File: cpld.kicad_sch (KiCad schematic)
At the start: 9 parts, among them J2 Conn_01x06_Pin, U6 ATF1508AS-10AU100

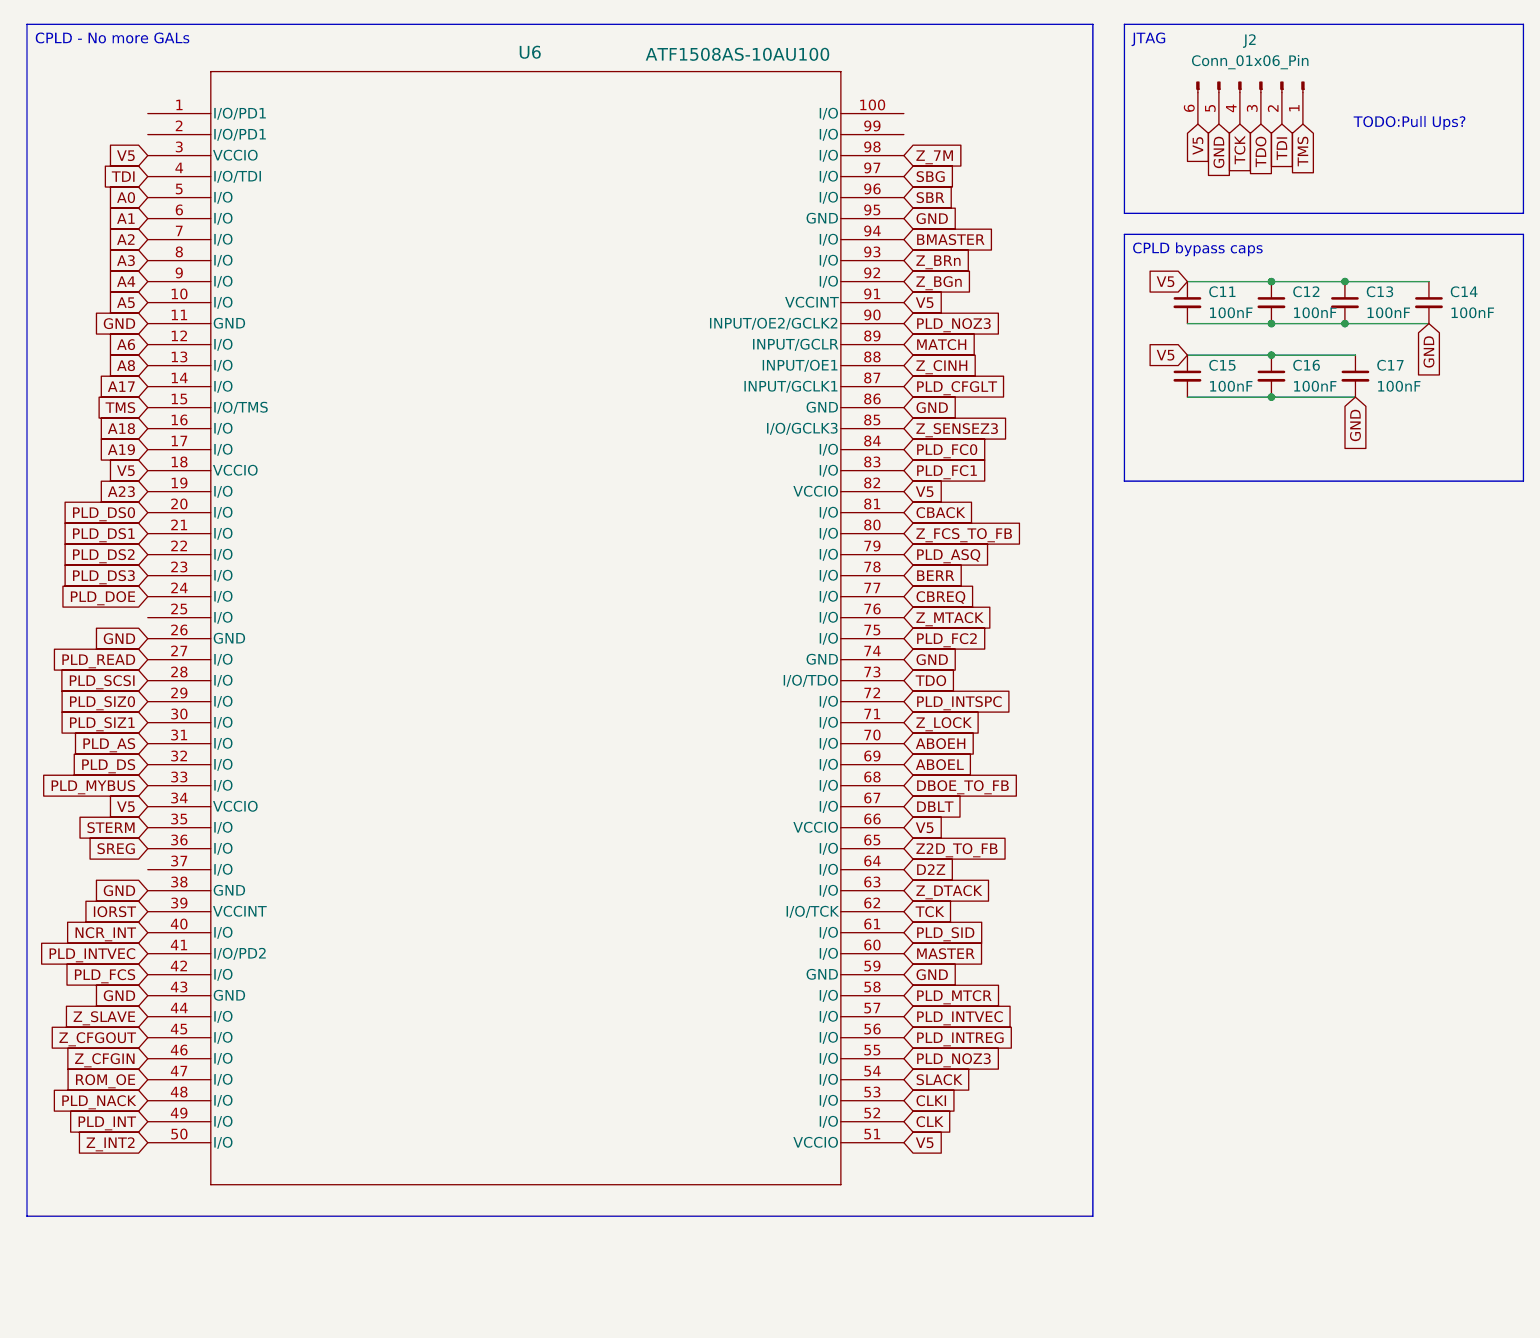
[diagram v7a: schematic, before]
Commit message: Incorporate Feedback from LIV2
- Move CLK, CLKI, Z_7M to GCLK1, GCLK2, GCLK3
  as they are connected to all macro cells.
- OE1 and GCLR on the 1508 are input only, move FC0/FC1 there.

Also found two duplicate signals on the ATF1508, consolidated them.
This leaves us with 8 free I/Os at the moment.
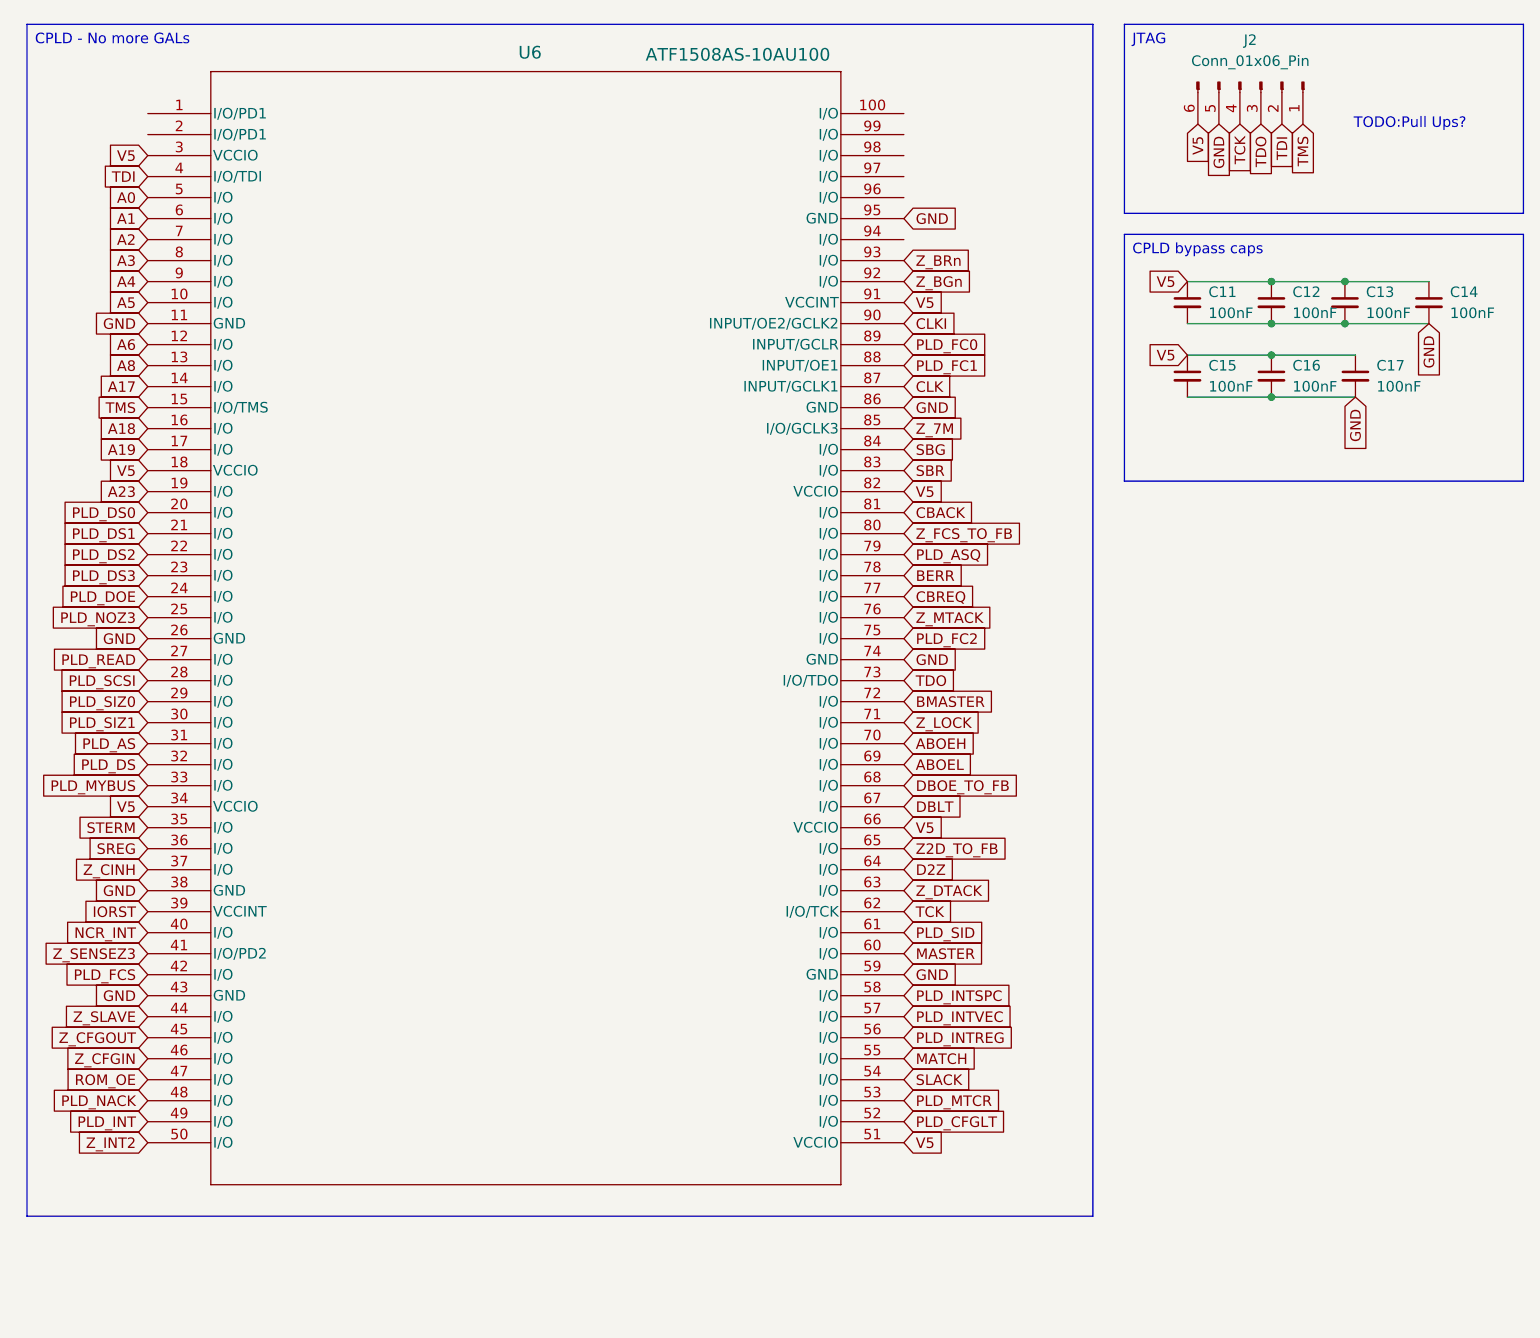
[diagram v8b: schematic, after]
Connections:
- net BMASTER: now also U6.72 (I/O); no longer U6.94 (I/O)
- net CLK: now also U6.87 (INPUT/GCLK1); no longer U6.52 (I/O)
- net CLKI: now also U6.90 (INPUT/OE2/GCLK2); no longer U6.53 (I/O)
- net MATCH: now also U6.55 (I/O); no longer U6.89 (INPUT/GCLR)
- net PLD_CFGLT: now also U6.52 (I/O); no longer U6.87 (INPUT/GCLK1)
- net PLD_FC0: now also U6.89 (INPUT/GCLR); no longer U6.84 (I/O)
- net PLD_FC1: now also U6.88 (INPUT/OE1); no longer U6.83 (I/O)
- net PLD_INTSPC: now also U6.58 (I/O); no longer U6.72 (I/O)
- net PLD_INTVEC: no longer U6.41 (I/O/PD2)
- net PLD_MTCR: now also U6.53 (I/O); no longer U6.58 (I/O)
- net PLD_NOZ3: now also U6.25 (I/O); no longer U6.55 (I/O), U6.90 (INPUT/OE2/GCLK2)
- net SBG: now also U6.84 (I/O); no longer U6.97 (I/O)
- net SBR: now also U6.83 (I/O); no longer U6.96 (I/O)
- net Z_7M: now also U6.85 (I/O/GCLK3); no longer U6.98 (I/O)
- net Z_CINH: now also U6.37 (I/O); no longer U6.88 (INPUT/OE1)
- net Z_SENSEZ3: now also U6.41 (I/O/PD2); no longer U6.85 (I/O/GCLK3)
